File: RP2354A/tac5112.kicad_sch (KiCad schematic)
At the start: 8 parts, among them U301 TAC5112

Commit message: First cut at BOM selection for caps and resistors
The size choices were a bit random, this standardizes on 0402 for
resistors.  Also, optimize the BOM by just sharing values where they
don't matter that much.

For example, we need those 5k1 resistors for the USB CC pulldowns, and
we might as well then use that for the i2c pullup resistors too.  And
the self-biasing source resistor for the JFET input could use the same.

For similar reasons, just standardize on 33R for the low value resistors
that we use for the USB data line serial termination and the analog
voltage RC filtering.

Capacitors are 0402 for small values (0.1uF and smaller) or 0603 for
bigger capacitance values.  That seems to match availability.

Signed-off-by: Linus Torvalds <torvalds@linux-foundation.org>
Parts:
- C301, C302, C305: footprint Capacitor_SMD:C_0805_2012Metric -> Capacitor_SMD:C_0603_1608Metric
- C307: footprint Capacitor_SMD:C_0402_1005Metric -> Capacitor_SMD:C_0603_1608Metric
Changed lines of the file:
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@@
 			)
 		)
-		(property "Footprint" "Capacitor_SMD:C_0805_2012Metric"
+		(property "Footprint" "Capacitor_SMD:C_0603_1608Metric"
 			(at 136.1948 38.1 0)
 			(effects
@@
 			)
 		)
-		(property "Footprint" "Capacitor_SMD:C_0402_1005Metric"
+		(property "Footprint" "Capacitor_SMD:C_0603_1608Metric"
 			(at 164.7952 38.1 0)
 			(effects
@@
 			)
 		)
-		(property "Footprint" "Capacitor_SMD:C_0805_2012Metric"
+		(property "Footprint" "Capacitor_SMD:C_0603_1608Metric"
 			(at 47.9552 38.1 0)
 			(effects
@@
 			)
 		)
-		(property "Footprint" "Capacitor_SMD:C_0805_2012Metric"
+		(property "Footprint" "Capacitor_SMD:C_0603_1608Metric"
 			(at 64.4652 38.1 0)
 			(effects

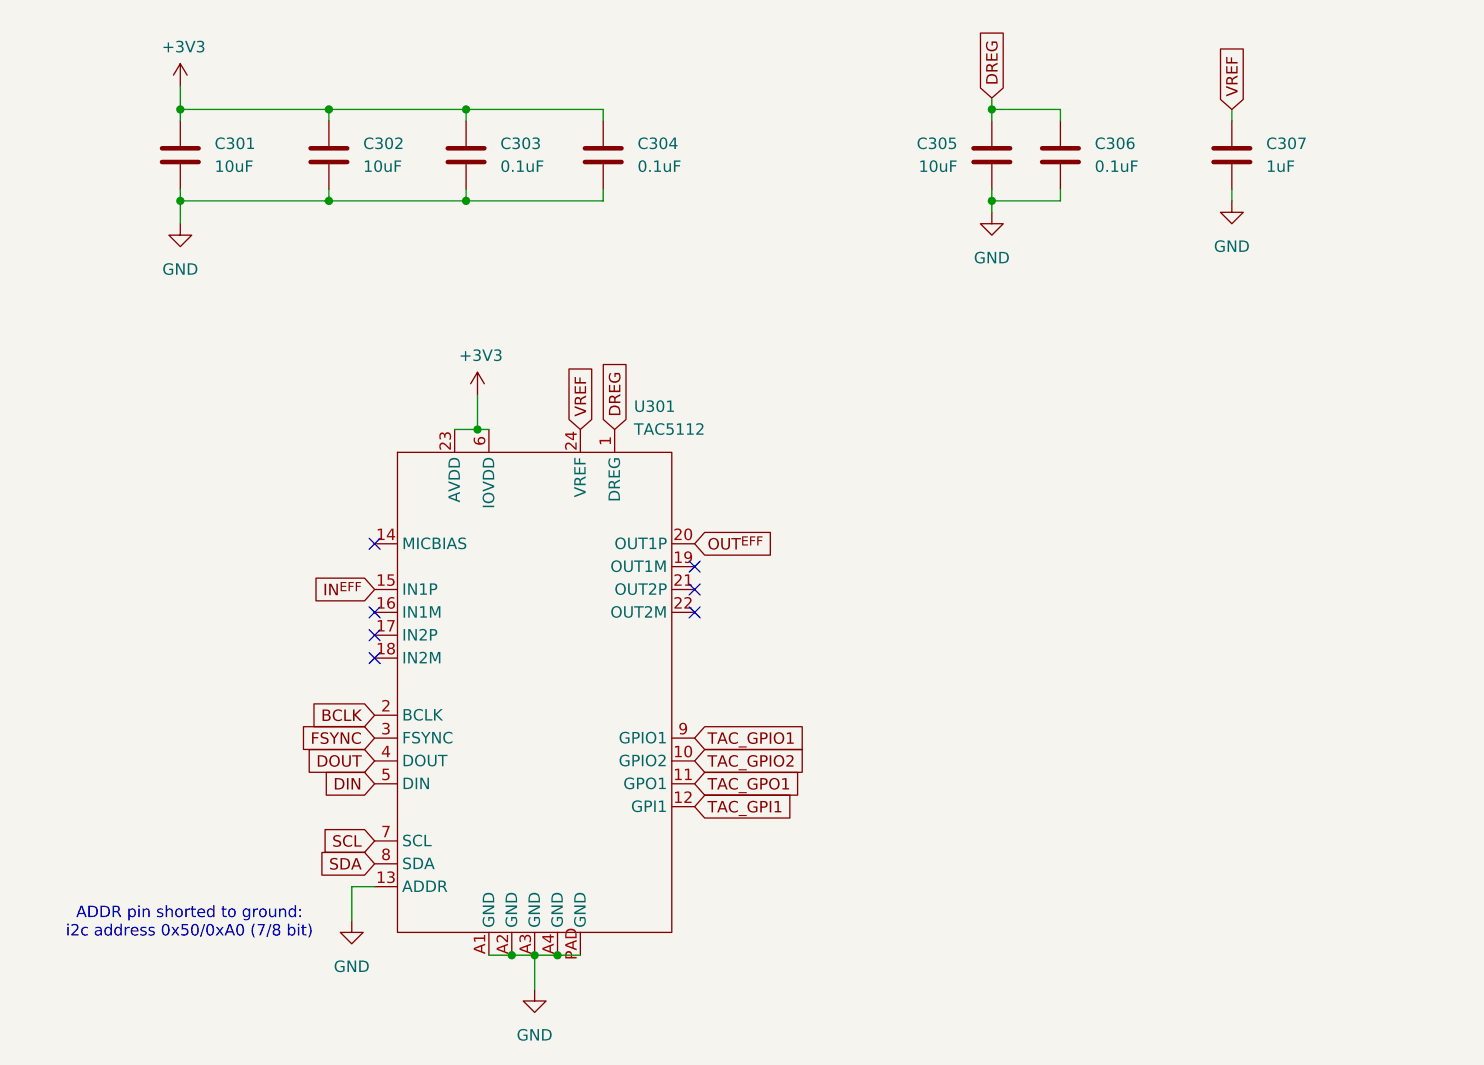
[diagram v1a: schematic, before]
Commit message: Switch the MMBF5103 JFET over to a OPA365 op amp
This is a long time coming, but it was triggered by jlcpcb not stocking
the MMBF5103, and all the alternatives looked worse.  So I guess sanity
has to prevail, and I should use an opamp rather than a discrete JFET
input stage.

I looked at the J201 - which I have tested and works, but has a
potentially very low V_{GSOFF} that will cause clipping.  And the
MMBFJ309L looked good in simulation and had better parameter values, but
I've never tested it, so it seemed a bit risky particularly since the
intended market seems to be for much higher frequency circuits.

I even looked at the JFE150, which is another silly-expensive thing sold
to audio markets.  I guess that tracks.

In the end, a plain simple opamp is definitely the sane choice.

To rebias the incoming signal, this uses the MICBIAS from the TAC5112,
which is typically 2.75V (but can be programmed to 2.5V or turned off
entirely etc).  It's there, it's almost what it is meant for, so let's
use it.

The OPA365 looks fine, and does rail-to-rail input and output and can do
single supplies down to 2.2V, but rather than put even more on the 3.3V
rail (and limiting the voltage swing), this just uses the 5V USB VBUS
power supply.

This does have some minimal caps for filtering (replacing the old +VA
supply to the JFET) but the OPA365 also claims good PSRR.

This all does seem like the right thing to do, but I'm still a bit sad
since the discrete JFET was just more interesting.

Signed-off-by: Linus Torvalds <torvalds@linux-foundation.org>
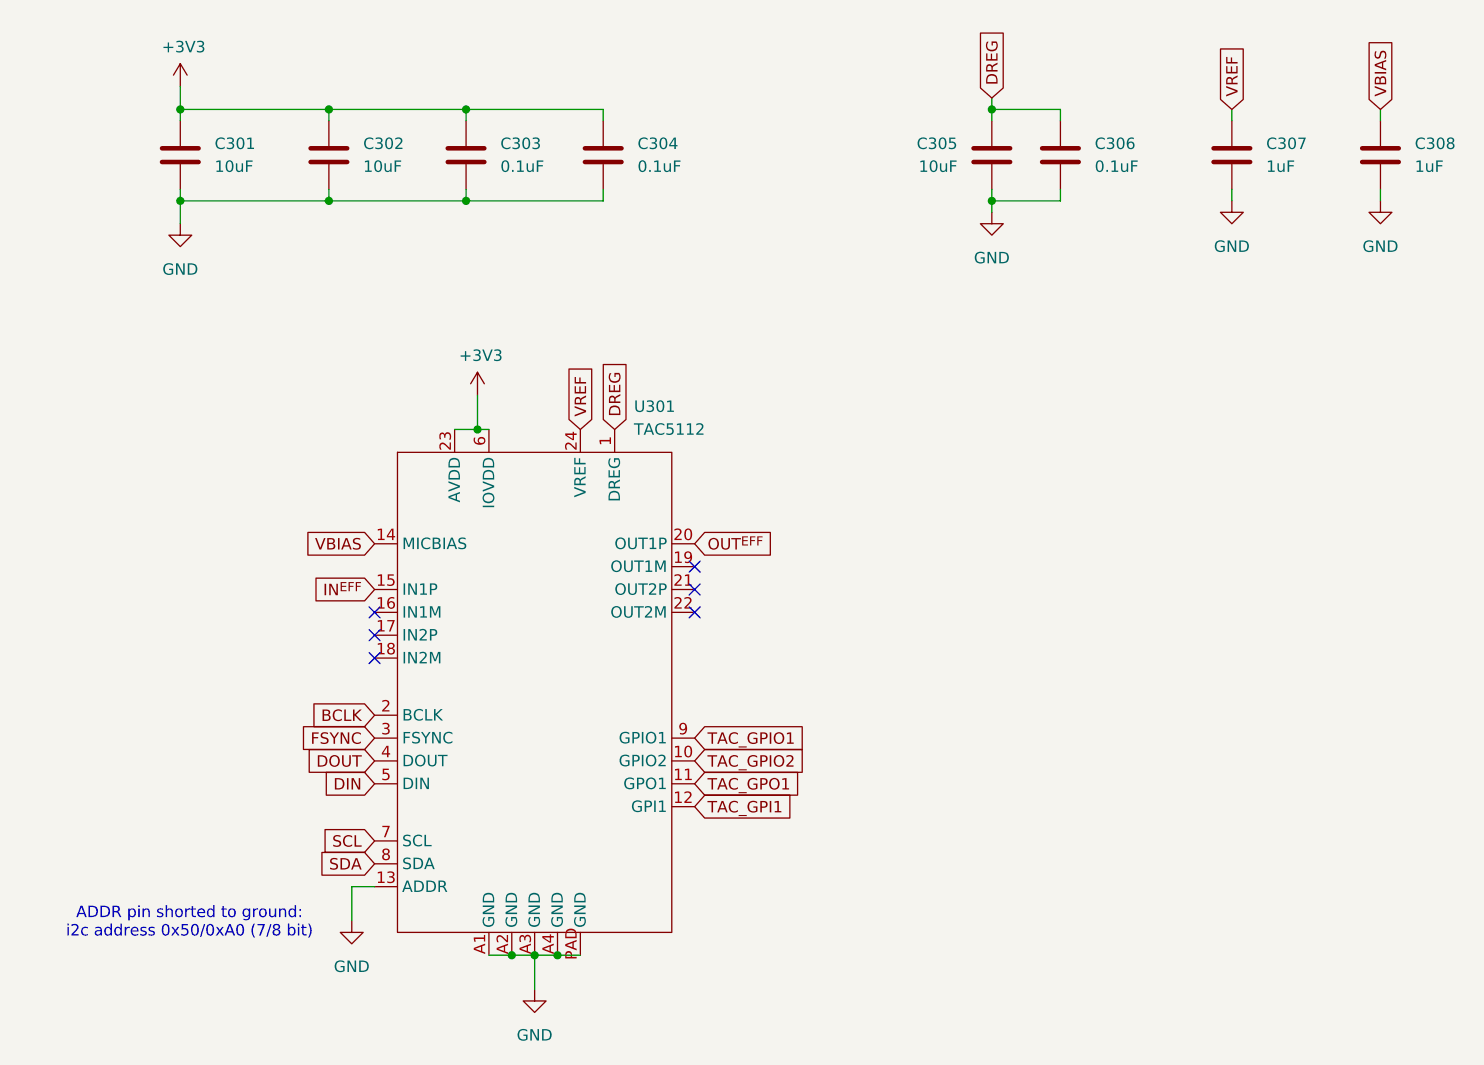
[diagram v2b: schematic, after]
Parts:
- added C308: 1uF, Capacitor_SMD:C_0603_1608Metric, symbol Device:C
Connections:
- net GND: now also C308.2
- net VBIAS: now reaches U301.14 (MICBIAS)
- net VBIAS: now also C308.1
- no-connect marks 7 -> 6
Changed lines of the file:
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@@
-	)
-	(no_connect
-		(at 68.58 77.47)
 	)
 	(no_connect
@@
 	(wire
 		(pts
+			(xy 180.34 30.48) (xy 180.34 29.21)
+		)
+		(stroke
+			(width 0)
+			(type default)
+		)
+	)
+	(wire
+		(pts
 			(xy 83.82 123.19) (xy 86.36 123.19)
 		)
@@
 	(wire
 		(pts
+			(xy 180.34 39.37) (xy 180.34 38.1)
+		)
+		(stroke
+			(width 0)
+			(type default)
+		)
+	)
+	(wire
+		(pts
 			(xy 137.16 39.37) (xy 144.78 39.37)
 		)
@@
 		)
 	)
+	(global_label "VBIAS"
+		(shape input)
+		(at 180.34 29.21 90)
+		(fields_autoplaced yes)
+		(effects
+			(font
+				(size 1.27 1.27)
+			)
+			(justify left)
+		)
+		(property "Intersheetrefs" "${INTERSHEET_REFS}"
+			(at 180.34 20.9633 90)
+			(effects
+				(font
+					(size 1.27 1.27)
+				)
+				(justify left)
+				(hide yes)
+			)
+		)
+	)
 	(global_label "DREG"
 		(shape input)
@@
 				)
 				(justify left)
+				(hide yes)
+			)
+		)
+	)
+	(global_label "VBIAS"
+		(shape input)
+		(at 68.58 77.47 180)
+		(fields_autoplaced yes)
+		(effects
+			(font
+				(size 1.27 1.27)
+			)
+			(justify right)
+		)
+		(property "Intersheetrefs" "${INTERSHEET_REFS}"
+			(at 60.3333 77.47 0)
+			(effects
+				(font
+					(size 1.27 1.27)
+				)
+				(justify right)
 				(hide yes)
 			)
@@
 				(path "/9e337e0b-885b-4d2b-99a2-62cdd082c615/d22a6a21-f0d7-406e-8a6d-681cd127beec"
 					(reference "#PWR0305")
+					(unit 1)
+				)
+			)
+		)
+	)
+	(symbol
+		(lib_id "power:GND")
+		(at 180.34 39.37 0)
+		(unit 1)
+		(exclude_from_sim no)
+		(in_bom yes)
+		(on_board yes)
+		(dnp no)
+		(fields_autoplaced yes)
+		(property "Reference" "#PWR0313"
+			(at 180.34 45.72 0)
+			(effects
+				(font
+					(size 1.27 1.27)
+				)
+				(hide yes)
+			)
+		)
+		(property "Value" "GND"
+			(at 180.34 44.45 0)
+			(effects
+				(font
+					(size 1.27 1.27)
+				)
+			)
+		)
+		(property "Footprint" ""
+			(at 180.34 39.37 0)
+			(effects
+				(font
+					(size 1.27 1.27)
+				)
+				(hide yes)
+			)
+		)
+		(property "Datasheet" ""
+			(at 180.34 39.37 0)
+			(effects
+				(font
+					(size 1.27 1.27)
+				)
+				(hide yes)
+			)
+		)
+		(property "Description" "Power symbol creates a global label with name \"GND\" , ground"
+			(at 180.34 39.37 0)
+			(effects
+				(font
+					(size 1.27 1.27)
+				)
+				(hide yes)
+			)
+		)
+		(pin "1"
+		)
+		(instances
+			(project "RP2354A"
+				(path "/9e337e0b-885b-4d2b-99a2-62cdd082c615/d22a6a21-f0d7-406e-8a6d-681cd127beec"
+					(reference "#PWR0313")
 					(unit 1)
 				)
@@
 					(unit 1)
 				)
+			)
+		)
+	)
+	(symbol
+		(lib_id "Device:C")
+		(at 180.34 34.29 0)
+		(unit 1)
+		(exclude_from_sim no)
+		(in_bom yes)
+		(on_board yes)
+		(dnp no)
+		(fields_autoplaced yes)
+		(property "Reference" "C308"
+			(at 184.15 33.0199 0)
+			(effects
+				(font
+					(size 1.27 1.27)
+				)
+				(justify left)
+			)
+		)
+		(property "Value" "1uF"
+			(at 184.15 35.5599 0)
+			(effects
+				(font
+					(size 1.27 1.27)
+				)
+				(justify left)
+			)
+		)
+		(property "Footprint" "Capacitor_SMD:C_0603_1608Metric"
+			(at 181.3052 38.1 0)
+			(effects
+				(font
+					(size 1.27 1.27)
+				)
+				(hide yes)
+			)
+		)
+		(property "Datasheet" "~"
+			(at 180.34 34.29 0)
+			(effects
+				(font
+					(size 1.27 1.27)
+				)
+				(hide yes)
+			)
+		)
+		(property "Description" "Unpolarized capacitor"
+			(at 180.34 34.29 0)
+			(effects
+				(font
+					(size 1.27 1.27)
+				)
+				(hide yes)
+			)
+		)
+		(pin "2"
+		)
+		(pin "1"
+		)
+		(instances
+			(project "RP2354A"
+				(path "/9e337e0b-885b-4d2b-99a2-62cdd082c615/d22a6a21-f0d7-406e-8a6d-681cd127beec"
+					(reference "C308")
+					(unit 1)
+				)

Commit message: rp2354: First stab at pcb layout
This is an insane 6-layer stackup, not because I need six layers
(although it does allow me to be even lazier than usual), but because I
want to use via-in-pad and at that point jlcpcb pretty much ends up
doing the whole precision 6-layer thing anyway.

The minimal RP2354A board makes do with just a simple two-layer stackup,
and I'm sure this could have been done that way too.  But with four
layers it's easy to just use one layer for the +1V1 zone and one for the
+3V3 zone under the RP2354A, and just bring things in with the vias.

This is all connected, but with some ERC noise. Mostly harmless (tm).

Also add JLCPCB part numbers to things, although I need to check them
all several times.

Signed-off-by: Linus Torvalds <torvalds@linux-foundation.org>
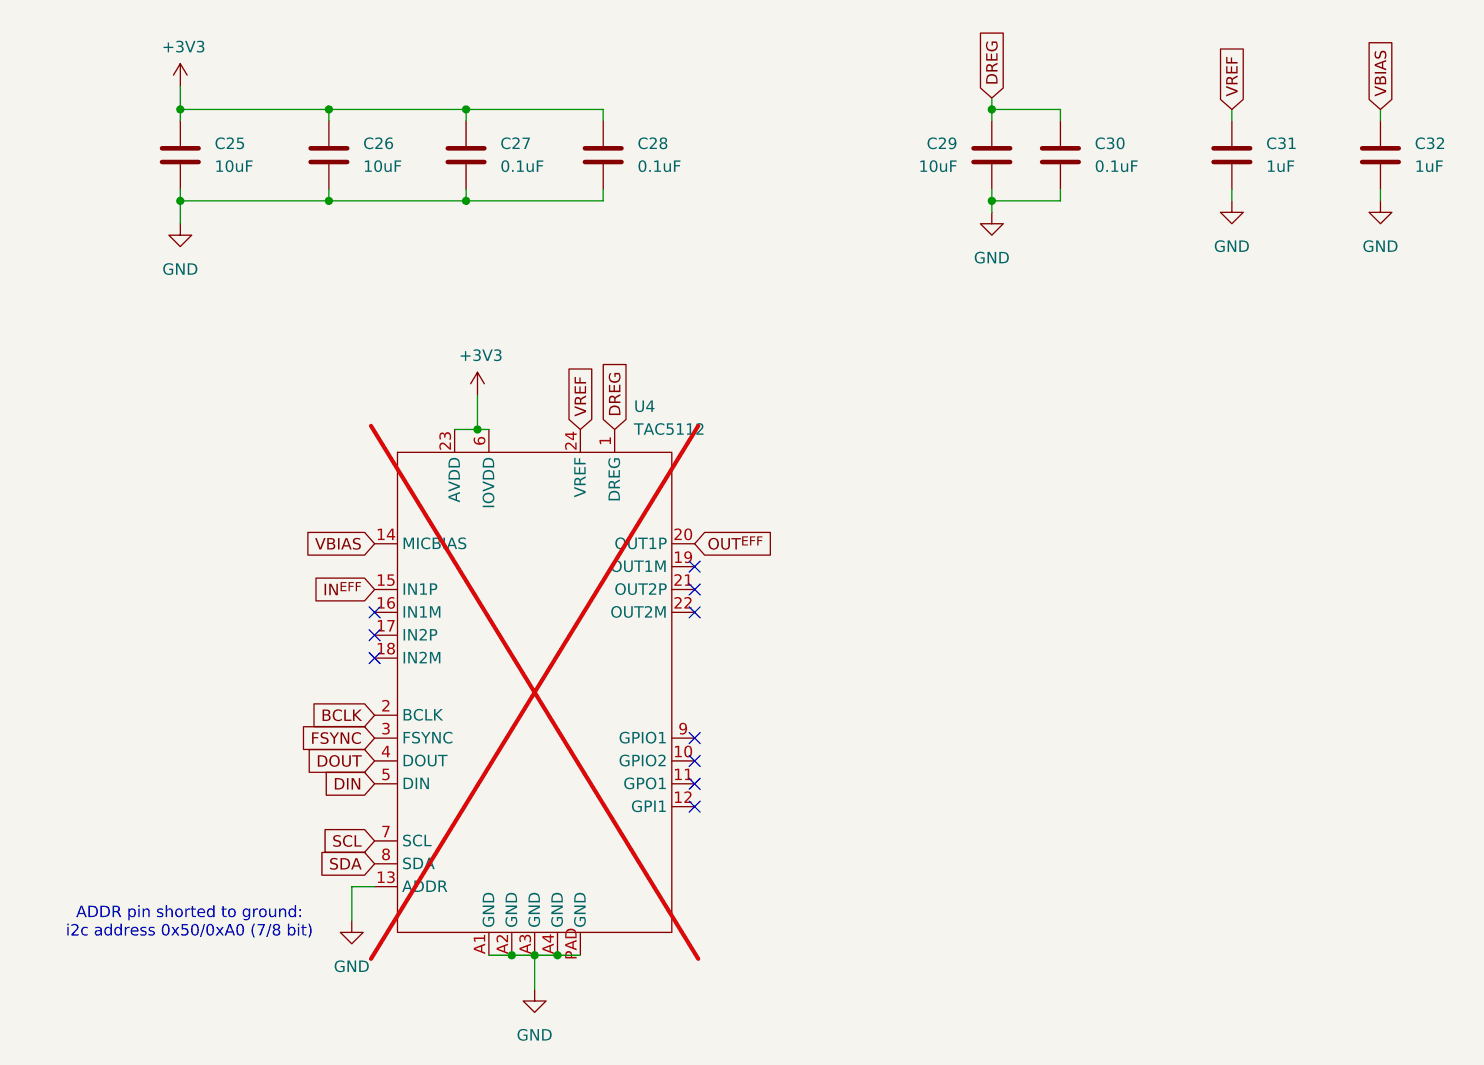
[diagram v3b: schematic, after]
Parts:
- C25: renamed from C301; JLCPCB (none) -> C91606
- C26: renamed from C302; JLCPCB (none) -> C91606
- C27: renamed from C303; JLCPCB (none) -> C1525
- C28: renamed from C304; JLCPCB (none) -> C1525
- C29: renamed from C305; JLCPCB (none) -> C91606
- C30: renamed from C306; JLCPCB (none) -> C1525
- C31: renamed from C307; JLCPCB (none) -> C519560
- C32: renamed from C308; JLCPCB (none) -> C519560
- U4: renamed from U301; now not fitted
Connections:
- net TAC_GPI1: no longer names the net of U4.12 (GPI1)
- net TAC_GPIO1: no longer names the net of U4.9 (GPIO1)
- net TAC_GPIO2: no longer names the net of U4.10 (GPIO2)
- net TAC_GPO1: no longer names the net of U4.11 (GPO1)
- no-connect marks 6 -> 10

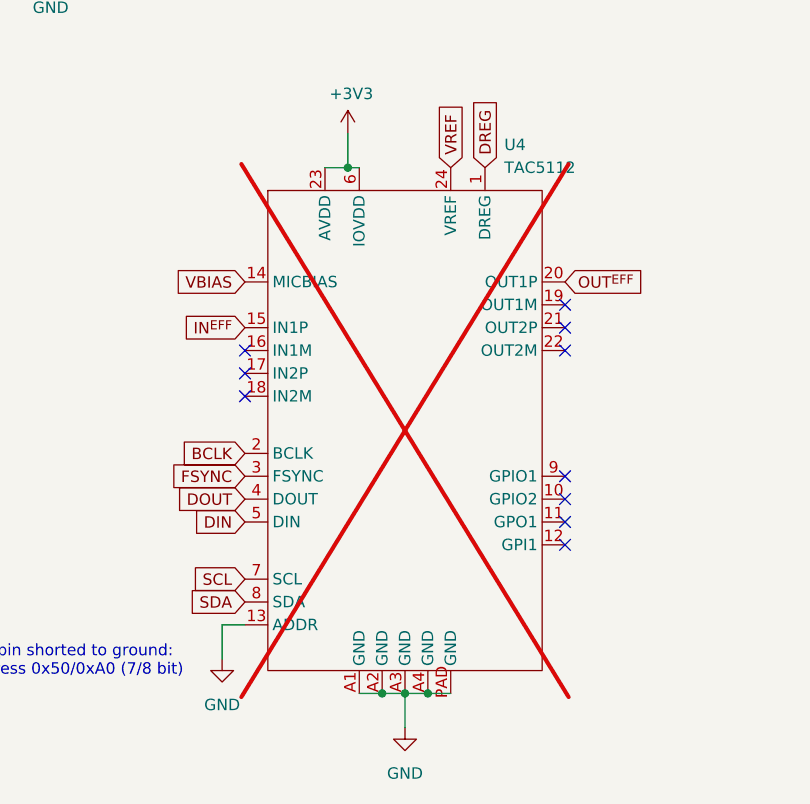
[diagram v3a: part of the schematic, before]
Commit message: Fix missing JLCPCB number, and replace "DNP" with "not in BOM"
Also cross-verify the JLCPCB numbers.

Signed-off-by: Linus Torvalds <torvalds@linux-foundation.org>
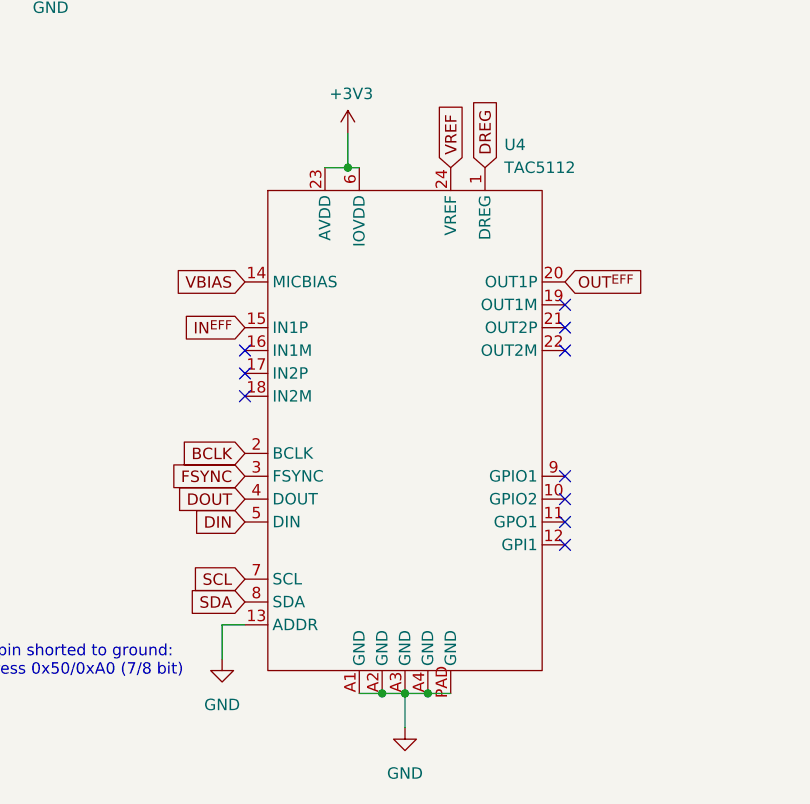
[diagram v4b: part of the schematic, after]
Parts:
- U4: JLCPCB (none) -> C44853692; now fitted
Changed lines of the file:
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@@
 		(in_bom yes)
 		(on_board yes)
-		(dnp yes)
+		(dnp no)
 		(fields_autoplaced yes)
 		(property "Reference" "U4"
@@
 			)
 		)
-		(property "JLCPCB" ""
+		(property "JLCPCB" "C44853692"
 			(at 86.36 93.98 0)
 			(effects
